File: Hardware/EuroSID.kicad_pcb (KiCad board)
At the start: 2 copper layers, 213.3 x 106.6 mm, 232 parts, among them J1 GATE_2, J10 IN_2, J11 IN_3, J12 PWM_CV, J13 EXT_CON, J14 Conn_01x04_Female, J15 Eurorack Connector, J16 Conn_01x06_Male, J17 Conn_ARM_JTAG_SWD_10, J18 Power_Connector_IO, J19 Power_Connector, J2 GATE_3, J20 Digital_Connector_IO, J21 CV_Connector_IO, J22 Pot_Connector_IO, J23 Attenuverter_Connector_IO, J24 Digital_Connector, J25 CV_Connector, J26 Pot_Connector, J27 Attenuverter_Connector, J28 SID_Audio_Connector_IO, J29 SID_Audio_Connector, J3 GATE_1, J4 OUT2_CON, J5 CUTOFF_CV, J6 SHAPE_CV, J7 SET_CV, J8 OUT1_CON, J9 IN_1, Q1 MMBT3904, Q2 MMBT3904, Q3 MMBT3904, SW1 Frequency Adjust, SW10 SET_SW, SW11 FILTER_SW, SW12 FILTEREXT_SW, SW13 SHAPE_SW, SW2 MOD_SW, SW3 FILTER1_SW, SW4 PROG, SW5 VOICE_SW, SW6 FILTER2_SW, SW7 RST, SW8 MODE_SW, SW9 FILTER3_SW, U1 TLC5947DAP, U10 LM1117-3.3, U11 LM1117-5.0, U12 L7809, U13 STM32F303RBTx, U2 OPA1678, U3 MCP6004, U4 MCP6004, U6 74HC595, U7 74HC595, U8 SID, U9 LM1117-3.3, X1 ECS-8FMX-010-TR

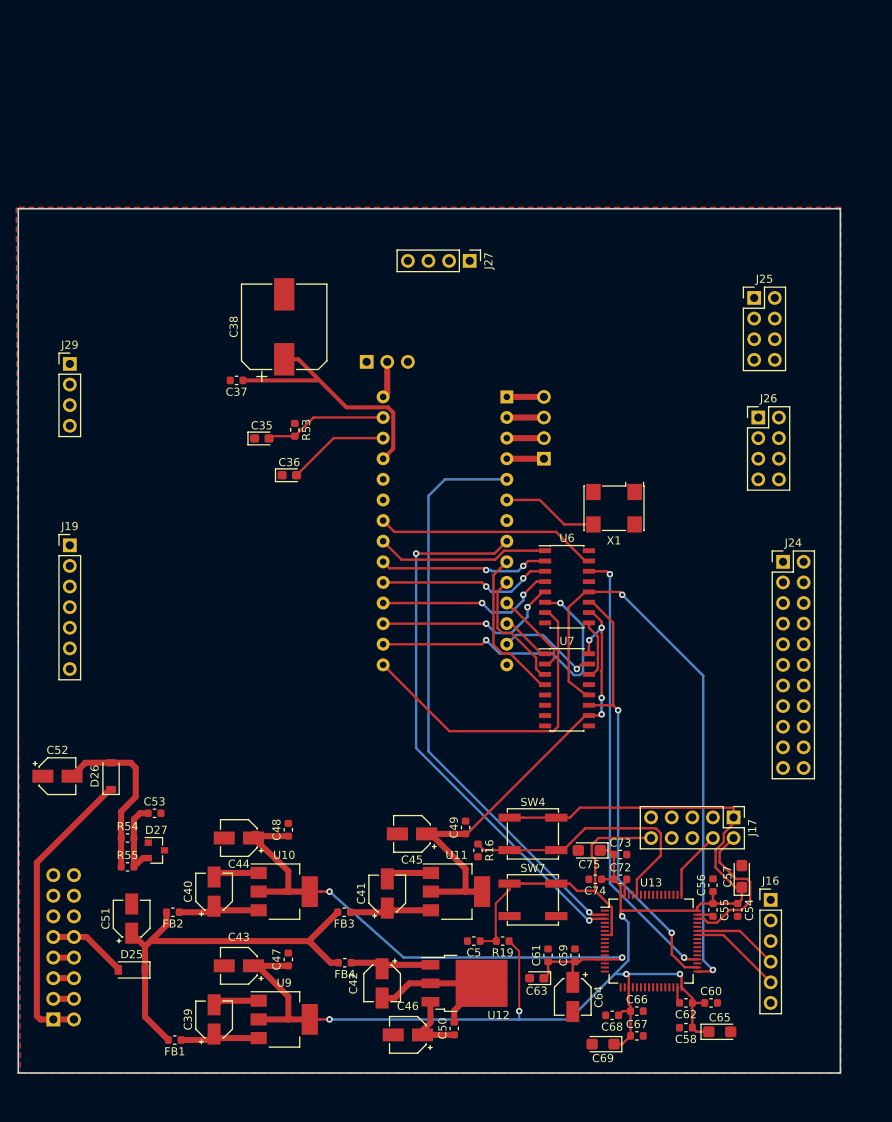
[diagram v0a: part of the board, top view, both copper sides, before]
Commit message: Added standof holes
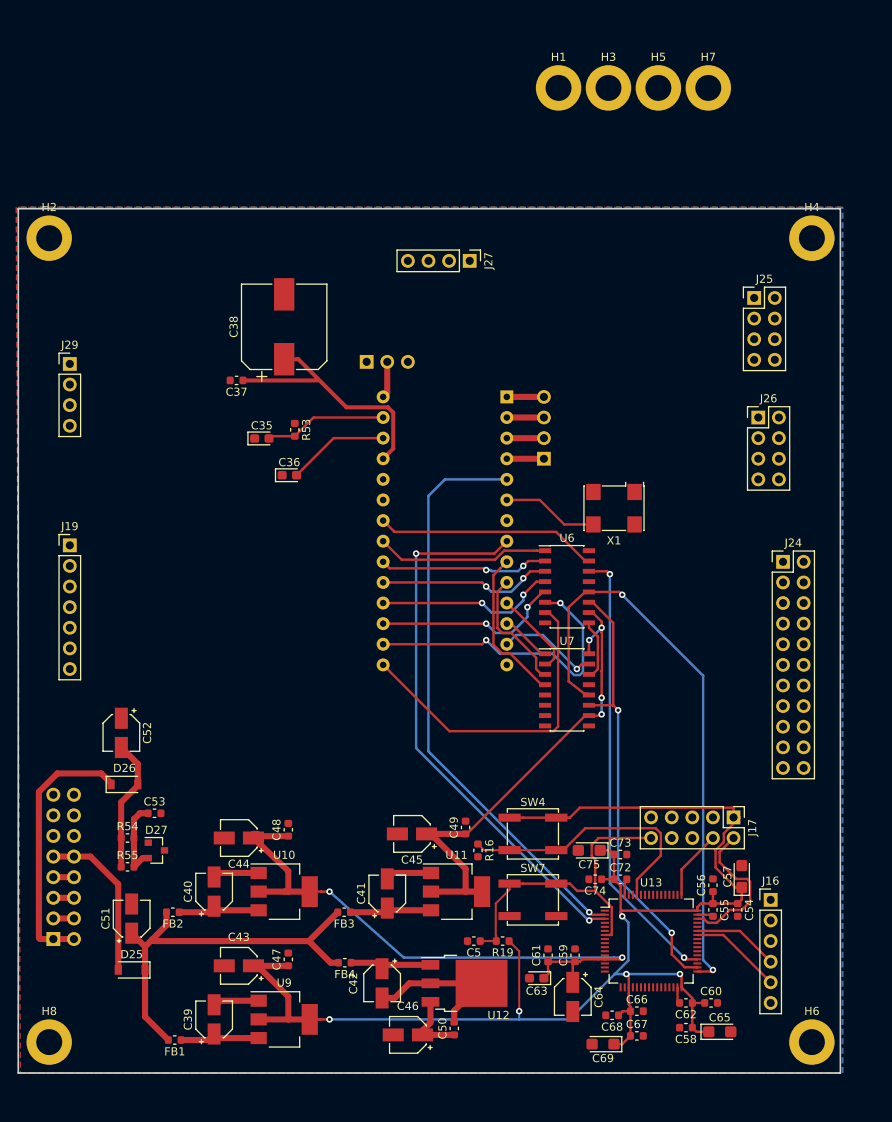
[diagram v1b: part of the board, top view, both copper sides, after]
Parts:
- added H1: MountingHole_Pad, MountingHole:MountingHole_3.2mm_M3_DIN965_Pad, F.Cu at (107.8, 21.6)
- added H2: MountingHole_Pad, MountingHole:MountingHole_3.2mm_M3_DIN965_Pad, F.Cu at (45.0, 40.1)
- added H3: MountingHole_Pad, MountingHole:MountingHole_3.2mm_M3_DIN965_Pad, F.Cu at (113.9, 21.6)
- added H4: MountingHole_Pad, MountingHole:MountingHole_3.2mm_M3_DIN965_Pad, F.Cu at (139.0, 40.1)
- added H5: MountingHole_Pad, MountingHole:MountingHole_3.2mm_M3_DIN965_Pad, F.Cu at (120.1, 21.6)
- added H6: MountingHole_Pad, MountingHole:MountingHole_3.2mm_M3_DIN965_Pad, F.Cu at (139.0, 139.2)
- added H7: MountingHole_Pad, MountingHole:MountingHole_3.2mm_M3_DIN965_Pad, F.Cu at (126.2, 21.6)
- added H8: MountingHole_Pad, MountingHole:MountingHole_3.2mm_M3_DIN965_Pad, F.Cu at (45.0, 139.2)
- moved J15 9.91 mm to (45.5, 126.5)
- moved C52 9.51 mm to (53.9, 101.1), turned to 270 degrees
- moved D26 1.94 mm to (54.3, 107.4), turned to 0 degrees
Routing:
- net Net-(D25-Pad2): track 9.77 -> 20.0 mm
- net -12V: track 21.7 -> 16.4 mm
- net Net-(D26-Pad1): track 36.5 -> 32.8 mm
- added copper zone on B.Cu, net GND

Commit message: Updated ADSR sliders
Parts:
- J15: footprint Connector_IDC:IDC-Header_2x08_P2.54mm_Vertical -> Connector_PinHeader_2.54mm:PinHeader_2x08_P2.54mm_Vertical
- J25, J26: footprint Connector_PinHeader_2.54mm:PinHeader_2x04_P2.54mm_Vertical -> Connector_PinSocket_2.54mm:PinSocket_2x04_P2.54mm_Vertical
- J27: footprint Connector_PinHeader_2.54mm:PinHeader_1x04_P2.54mm_Vertical -> Connector_PinSocket_2.54mm:PinSocket_1x04_P2.54mm_Vertical
- RV6: value SUSTAIN -> DECAY
- RV7: value DECAY -> SUSTAIN
- moved J20 159.4 mm to (171.2, 17.3)
- moved J21 159.4 mm to (189.5, 10.4)
- moved J22 159.4 mm to (205.3, 26.7)
- moved J23 159.4 mm to (193.1, 26.9)
- moved U1 159.4 mm to (206.3, 7.21)
- moved J18 159.4 mm to (156.6, 12.2)
- moved J28 159.4 mm to (157.4, 30.2)
- moved H6 130.1 mm to (81.8, 22.4)
- moved H8 119.3 mm to (61.5, 21.1)
- moved U4 41.6 mm to (239.7, 169.0)
- moved R56 31.3 mm to (275.7, 71.9)
- moved U6 31.2 mm to (78.0, 88.4)
- moved U2 27.1 mm to (208.8, 158.2)
- moved U3 26.3 mm to (220.7, 164.6)
- moved H4 19.7 mm to (133.9, 21.1)
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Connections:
- D11 pad 1: Net-(D11-Pad1) -> (no net)
- D17 pad 1: Net-(D17-Pad1) -> (no net)
- D22 pad 1: Net-(D22-Pad1) -> (no net)
- D5 pad 1: Net-(D5-Pad1) -> (no net)
- RV5 pad B: (no net) -> 3.3_IO
- RV5 pad E: (no net) -> Net-(RV5-PadE)
- RV6 pad 2: SUSTAIN_IO -> DECAY_IO
- RV6 pad B: (no net) -> 3.3_IO
- RV6 pad E: (no net) -> Net-(RV6-PadE)
- RV7 pad 2: DECAY_IO -> SUSTAIN_IO
- RV7 pad B: (no net) -> 3.3_IO
- RV7 pad E: (no net) -> Net-(RV7-PadE)
- RV8 pad B: (no net) -> 3.3_IO
- RV8 pad E: (no net) -> Net-(RV8-PadE)
- U1 pad 25: Net-(D5-Pad1) -> Net-(RV5-PadE)
- U1 pad 26: Net-(D11-Pad1) -> Net-(RV6-PadE)
- U1 pad 27: Net-(D17-Pad1) -> Net-(RV7-PadE)
- U1 pad 28: Net-(D22-Pad1) -> Net-(RV8-PadE)
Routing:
- net +5V: track 93.7 -> 159.0 mm, vias 4 -> 5
- net SID_CLK: track 54.7 -> 115.9 mm, vias 2 -> 4
- net SID_DATA: track 55.5 -> 105.3 mm, vias 2 -> 0
- net SID_LATCH: track 72.6 -> 117.5 mm, vias 2 -> 4
- net /SID Chip/D0: track 40.2 -> 11.8 mm, vias 0 -> 2
- net /SID Chip/D1: track 38.3 -> 12.4 mm
- net Net-(U6-Pad9): track 7.52 -> 28.2 mm
- net /SID Chip/A3: track 6.26 -> 19.3 mm
- net /SID Chip/D7: track 27.4 -> 15.3 mm, vias 0 -> 2
- net /SID Chip/D2: track 23.2 -> 11.8 mm
- net /SID Chip/D3: track 22.4 -> 12.4 mm
- net /SID Chip/D4: track 21.6 -> 12.5 mm, vias 2 -> 0
- net /SID Chip/D5: track 21.0 -> 13.0 mm, vias 2 -> 0
- net /SID Chip/A4: track 12.6 -> 4.99 mm, vias 1 -> 0
- net /SID Chip/D6: track 21.4 -> 13.9 mm
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
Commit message: Added 3D models
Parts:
- SW4, SW7: footprint Button_Switch_SMD:SW_SPST_EVPBF -> Button_Switch_SMD:SW_SPST_TL3342
- moved RV9 157.2 mm to (326.9, 192.5)
- moved J27 132.3 mm to (130.1, 170.9)
- moved RV3 125.8 mm to (326.9, 140.5)
- moved C1 124.8 mm to (322.9, 52.1)
- moved U2 124.8 mm to (281.2, 56.6)
- moved U4 124.8 mm to (312.1, 67.4)
- moved U3 124.8 mm to (293.1, 63.0)
- moved RV10 115.9 mm to (326.9, 159.5)
- moved J25 113.9 mm to (111.0, 159.5)
- moved RV1 109.3 mm to (326.9, 176.0)
- moved J26 106.9 mm to (88.2, 159.5)
- moved RV11 96.3 mm to (326.9, 122.7)
- moved J19 90.9 mm to (65.3, 167.1)
- moved J24 80.9 mm to (130.1, 160.8), turned to 90 degrees
- moved RV4 60.7 mm to (229.2, 163.3)
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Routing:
- net +5V: track 159.0 -> 237.8 mm, vias 5 -> 7
- net +3V3: track 180.9 -> 229.1 mm, vias 5 -> 7
- net +12V: track 49.5 -> 92.8 mm
- net GND: track 49.9 -> 86.9 mm, vias 0 -> 3
- net -10V_REF: track 10.1 -> 23.1 mm
- net -12V: track 16.4 -> 25.8 mm
- net SID_DATA: track 105.3 -> 106.1 mm

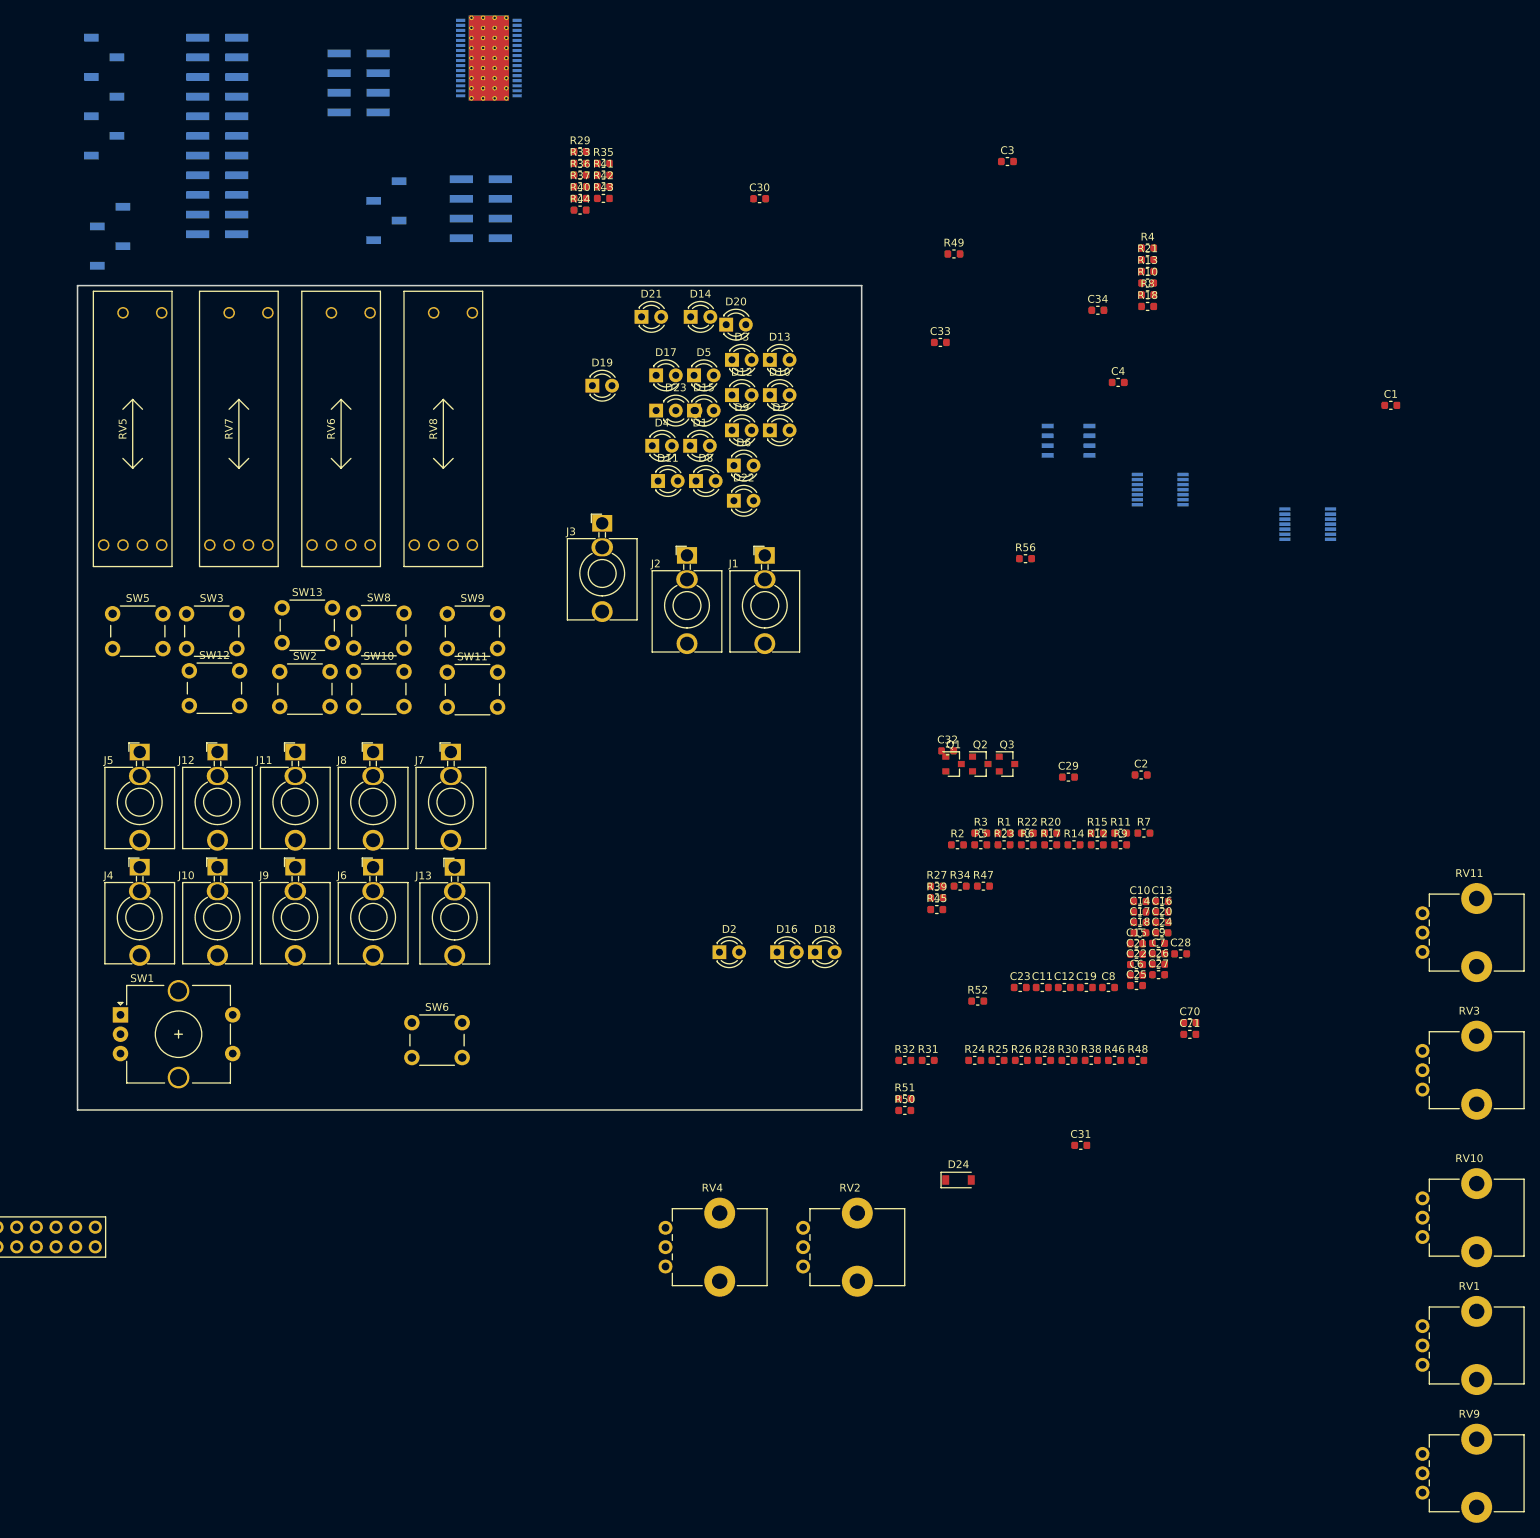
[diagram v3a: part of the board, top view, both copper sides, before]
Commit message: Finished mechanical design on PCB
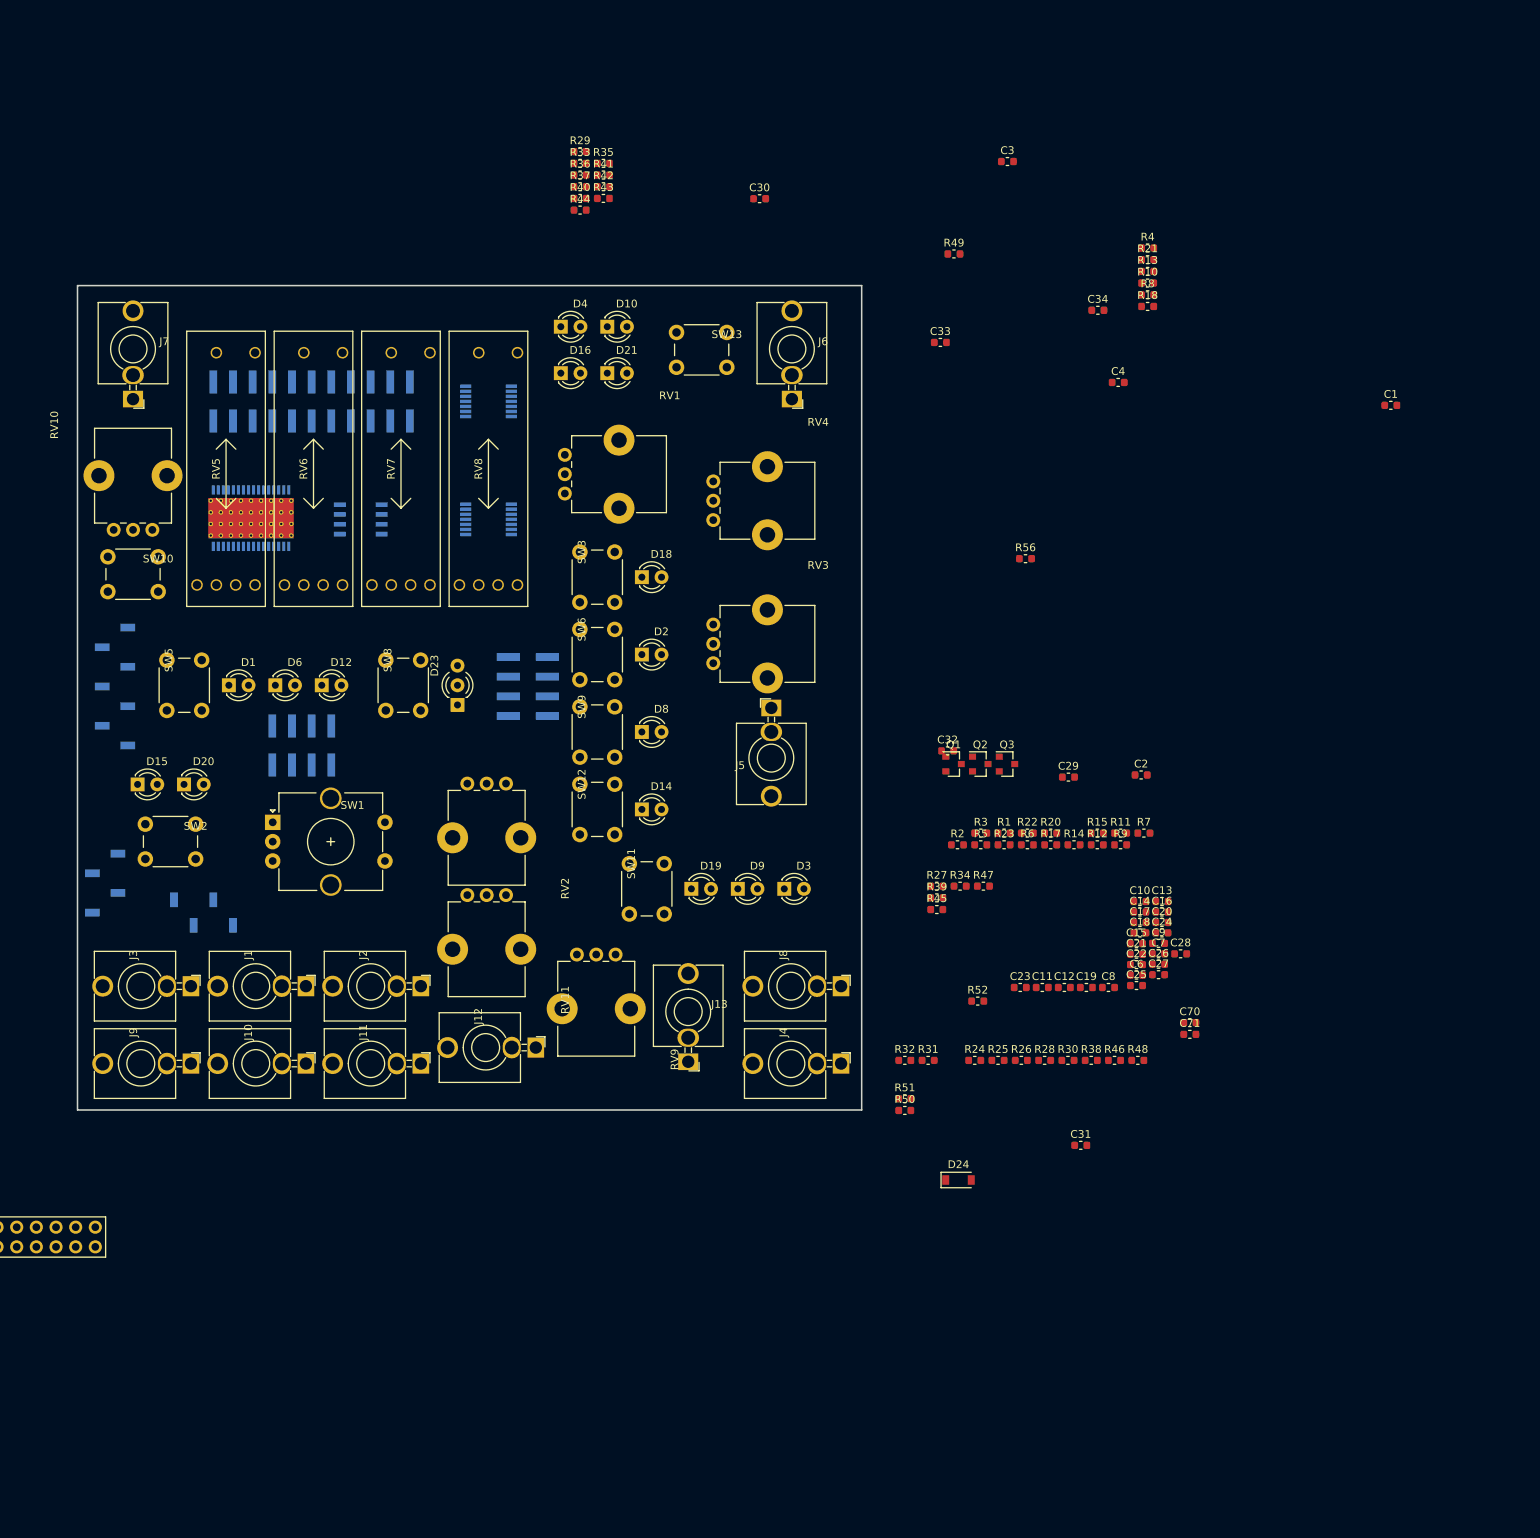
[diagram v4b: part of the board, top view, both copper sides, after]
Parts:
- removed D11: DECAY, LED_THT:LED_D3.0mm
- removed D13: SID2, LED_THT:LED_D3.0mm
- removed D17: SUSTAIN, LED_THT:LED_D3.0mm
- removed D22: RELEASE, LED_THT:LED_D3.0mm
- removed D5: ATTACK, LED_THT:LED_D3.0mm
- removed D7: SID1, LED_THT:LED_D3.0mm
- D21: value SYNC -> NOISE
- moved RV10 193.7 mm to (160.4, 60.7), turned to 90 degrees
- moved RV1 154.6 mm to (223.7, 61.0)
- moved RV9 123.4 mm to (220.2, 130.5), turned to 270 degrees
- moved RV11 120.9 mm to (206.1, 122.8), turned to 270 degrees
- moved U4 107.0 mm to (206.3, 51.6)
- moved RV3 101.9 mm to (242.8, 82.9)
- moved RV4 99.9 mm to (242.8, 64.4)
- moved J23 93.7 mm to (169.5, 117.6), turned to 90 degrees
- moved U2 92.0 mm to (189.8, 66.8)
- moved D20 90.9 mm to (168.2, 101.0)
- moved J4 88.0 mm to (245.5, 137.1), turned to 270 degrees
- moved U3 86.9 mm to (206.3, 66.8)
- moved J1 86.0 mm to (176.4, 127.1), turned to 270 degrees
- moved J6 86.0 mm to (245.5, 44.9), turned to 180 degrees
- moved D15 85.6 mm to (162.2, 101.0)
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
